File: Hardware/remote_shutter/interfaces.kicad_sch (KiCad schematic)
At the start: 12 parts, among them J2 OLED, J3 AudioJack3, Q1 DMN2056U, Q2 DMN2056U, SW1 RotaryEncoder_Switch

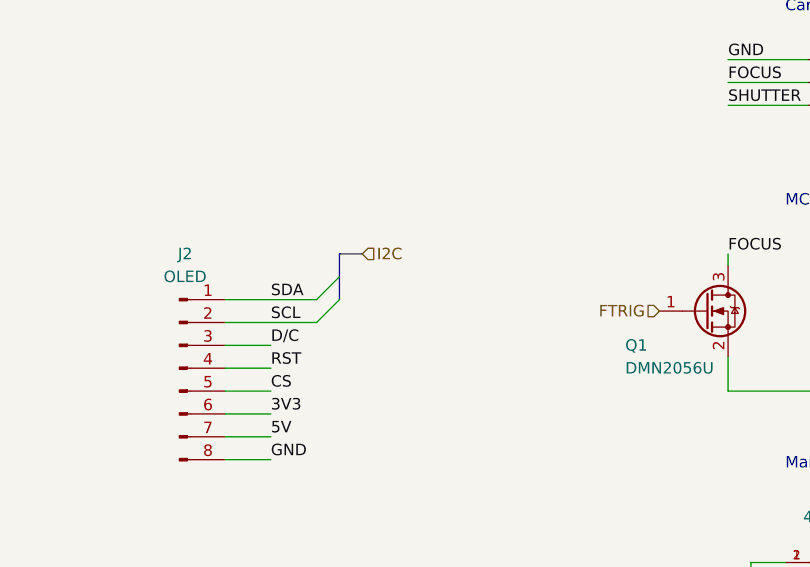
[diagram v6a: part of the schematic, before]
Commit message: Further routing. Fixed I2C net connection.
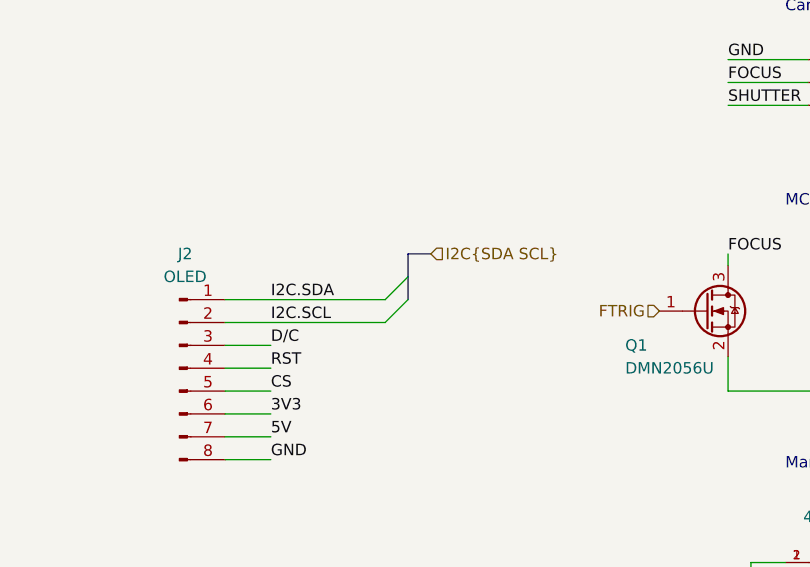
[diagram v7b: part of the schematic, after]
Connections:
- net SCL renamed I2C.SCL
- net SDA renamed I2C.SDA
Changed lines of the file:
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@@
   (junction (at 175.26 119.38) (diameter 0) (color 0 0 0 0)
   )
-  (bus_entry (at 127 73.66) (size 2.54 -2.54)
-    (stroke (width 0) (type default) (color 0 0 0 0))
-  )
-  (bus_entry (at 127 71.12) (size 2.54 -2.54)
+  (bus_entry (at 134.62 71.12) (size 2.54 -2.54)
+    (stroke (width 0) (type default) (color 0 0 0 0))
+  )
+  (bus_entry (at 134.62 73.66) (size 2.54 -2.54)
     (stroke (width 0) (type default) (color 0 0 0 0))
   )
@@
     (stroke (width 0) (type default) (color 0 0 0 0))
   )
-  (bus (pts (xy 129.54 71.12) (xy 129.54 68.58))
+  (bus (pts (xy 137.16 71.12) (xy 137.16 68.58))
     (stroke (width 0) (type default) (color 0 0 0 0))
   )
@@
     (stroke (width 0) (type default) (color 0 0 0 0))
   )
-  (bus (pts (xy 129.54 68.58) (xy 129.54 66.04))
+  (bus (pts (xy 137.16 68.58) (xy 137.16 66.04))
     (stroke (width 0) (type default) (color 0 0 0 0))
   )
@@
     (stroke (width 0) (type default) (color 0 0 0 0))
   )
-  (wire (pts (xy 116.84 71.12) (xy 127 71.12))
+  (wire (pts (xy 116.84 71.12) (xy 134.62 71.12))
     (stroke (width 0) (type default) (color 0 0 0 0))
   )
@@
     (stroke (width 0) (type default) (color 0 0 0 0))
   )
-  (bus (pts (xy 129.54 66.04) (xy 132.08 66.04))
+  (bus (pts (xy 137.16 66.04) (xy 139.7 66.04))
     (stroke (width 0) (type default) (color 0 0 0 0))
   )
@@
     (stroke (width 0) (type default) (color 0 0 0 0))
   )
-  (wire (pts (xy 116.84 73.66) (xy 127 73.66))
+  (wire (pts (xy 116.84 73.66) (xy 134.62 73.66))
     (stroke (width 0) (type default) (color 0 0 0 0))
   )
@@
     (effects (font (size 1.27 1.27)) (justify left bottom))
   )
-  (label "SDA" (at 121.92 71.12 0)
+  (label "I2C.SDA" (at 121.92 71.12 0)
     (effects (font (size 1.27 1.27)) (justify left bottom))
   )
@@
     (effects (font (size 1.27 1.27)) (justify left bottom))
   )
-  (label "SCL" (at 121.92 73.66 0)
+  (label "I2C.SCL" (at 121.92 73.66 0)
     (effects (font (size 1.27 1.27)) (justify left bottom))
   )
@@
     (effects (font (size 1.27 1.27)) (justify right))
   )
-  (hierarchical_label "I2C" (shape input) (at 132.08 66.04 0)
+  (hierarchical_label "I2C{SDA SCL}" (shape input) (at 139.7 66.04 0)
     (effects (font (size 1.27 1.27)) (justify left))
   )

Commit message: Fixed via sizes. Added IO0 pullup.
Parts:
- J2: footprint (none) -> Connector_PinSocket_2.54mm:PinSocket_1x08_P2.54mm_Vertical
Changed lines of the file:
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@@
     (property "Reference" "J2" (id 0) (at 112.395 66.04 0))
     (property "Value" "OLED" (id 1) (at 112.395 68.58 0))
-    (property "Footprint" "" (id 2) (at 111.76 78.74 0)
+    (property "Footprint" "Connector_PinSocket_2.54mm:PinSocket_1x08_P2.54mm_Vertical" (id 2) (at 111.76 78.74 0)
       (effects (font (size 1.27 1.27)) hide)
     )
